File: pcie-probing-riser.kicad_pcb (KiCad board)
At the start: 4 copper layers, 84 parts, among them U1 PCIexpress_x4, U2 PCIexpress_x8

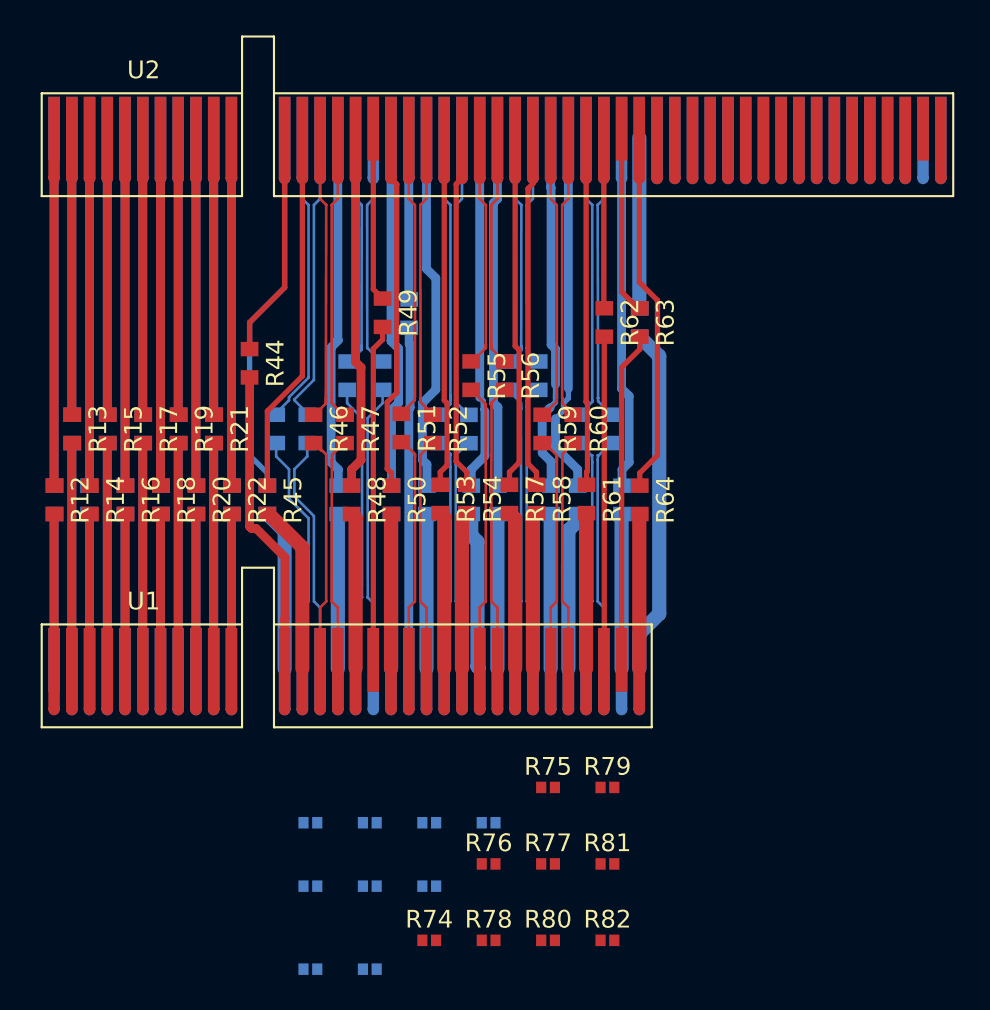
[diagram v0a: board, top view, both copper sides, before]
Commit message: Add resistors to ground and ground pour
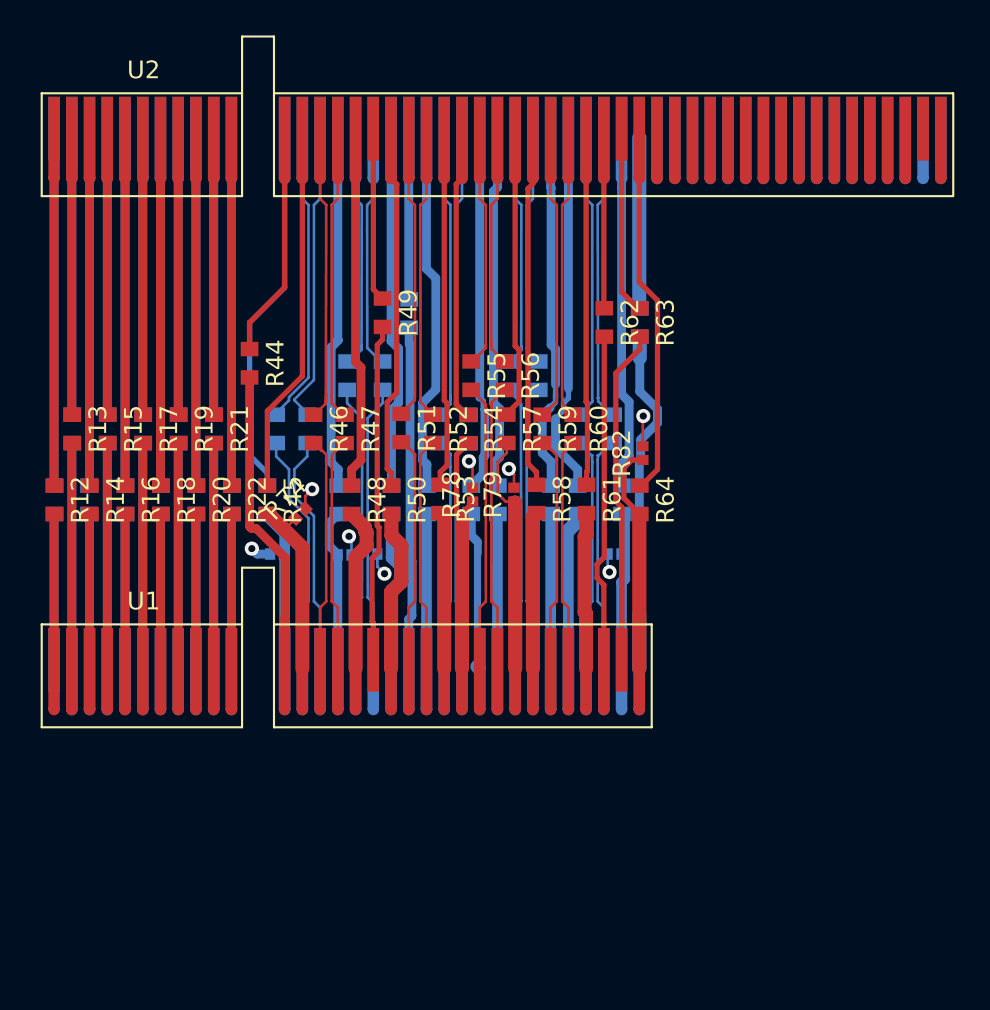
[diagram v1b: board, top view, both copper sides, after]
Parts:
- removed R68, R69, R70, R71, R72, R75, R76, R77, R80, R81: 0R, Resistor_SMD:R_0402_1005Metric
- moved R82 27.5 mm to (33.2, -11.6), turned to 90 degrees
- moved R78 25.2 mm to (23.6, -9.30), turned to 90 degrees
- moved R74 25.1 mm to (13.9, -8.23), turned to 45 degrees
- moved R66 18.8 mm to (16.4, -5.89)
- moved R79 17.3 mm to (25.9, -9.30), turned to 90 degrees
- moved R73 16.7 mm to (31.6, -5.94), turned to 180 degrees
- moved R65 15.3 mm to (12.5, -5.94), turned to 180 degrees
- moved R67 15.2 mm to (18.6, -5.94), turned to 180 degrees
- moved R57 3.96 mm to (25.5, -13.0)
- moved R54 3.94 mm to (23.3, -13.0)
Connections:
- net /PCIe_data/GNDA13 renamed /PCIe_data/GNDA12
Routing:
- net /PCIe_data/GNDB: track 0.00 -> 5.73 mm, vias 0 -> 4
- net /PCIe_data/GNDB22: track 8.89 -> 14.3 mm
- net /PCIe_data/GNDB25: track 8.91 -> 13.5 mm
- net /PCIe_data/GNDA: track 0.00 -> 4.61 mm, vias 0 -> 4
- net /PCIe_data/GNDB32: track 8.74 -> 13.0 mm
- net /PCIe_data/B25: track 17.6 -> 13.7 mm
- net /PCIe_data/B22: track 17.7 -> 13.8 mm
- net /PCIe_data/GNDA18: track 8.74 -> 11.4 mm
- net /PCIe_data/GNDA31: track 8.74 -> 11.1 mm
- net /PCIe_data/GNDA27: track 8.74 -> 11.0 mm
- net /PCIe_data/GNDA20: track 8.74 -> 11.0 mm
- net /PCIe_data/GNDA24: track 8.74 -> 11.0 mm
- net /PCIe_data/GNDA28: track 8.94 -> 10.3 mm
- net /PCIe_data/GNDA12: track 9.13 -> 10.4 mm
- net /PCIe_data/GNDB13: track 9.60 -> 10.5 mm
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- added copper zone on In2.Cu, net /PCIe_data/GNDA
- added copper zone on In1.Cu, net /PCIe_data/GNDB

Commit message: Switch x8 connector for x4. Add pours and edge cuts
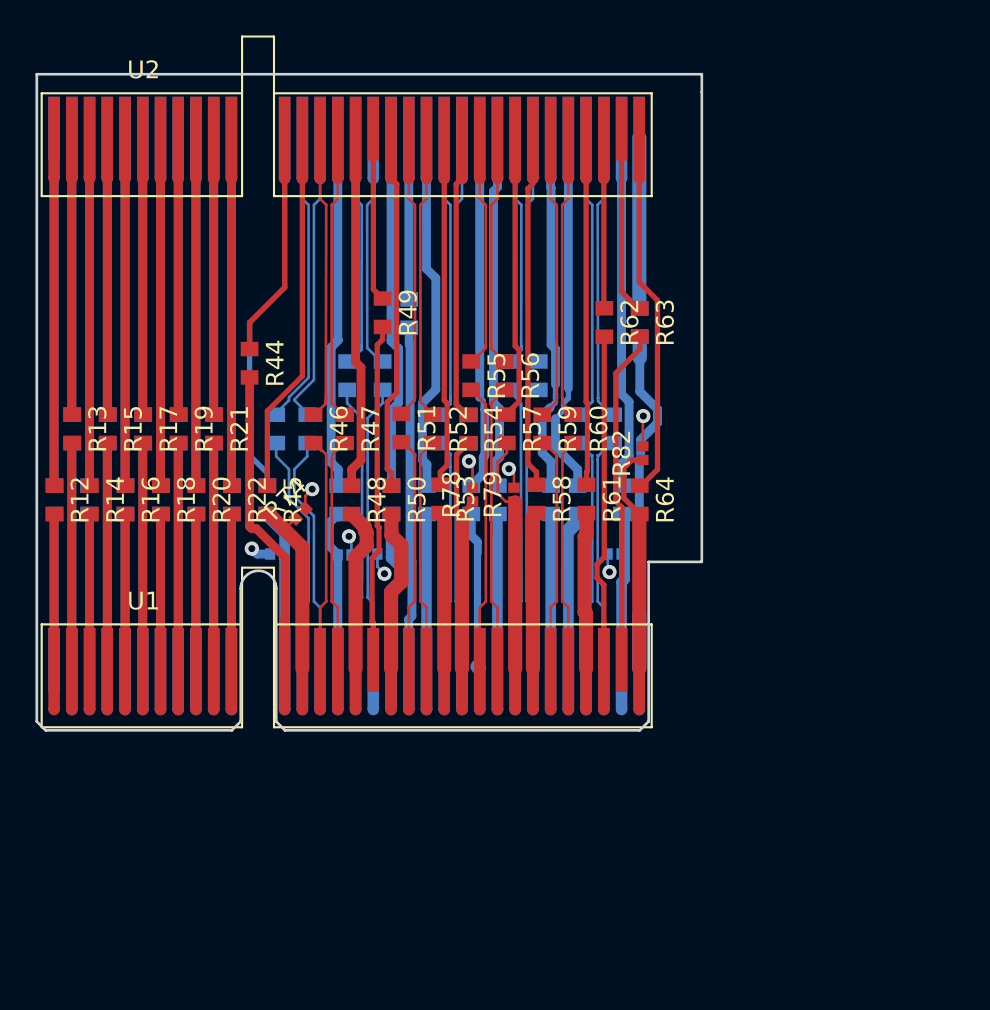
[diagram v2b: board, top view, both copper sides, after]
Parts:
- U2: value PCIexpress_x8 -> PCIexpress_x4; footprint Connector_PCBEdge:BUS_PCIexpress_x8 -> Connector_PCBEdge:BUS_PCIexpress_x4
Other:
- board outline added: 37.5 x 37 mm
